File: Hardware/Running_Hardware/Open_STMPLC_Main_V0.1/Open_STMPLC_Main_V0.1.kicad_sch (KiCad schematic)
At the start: 8 parts

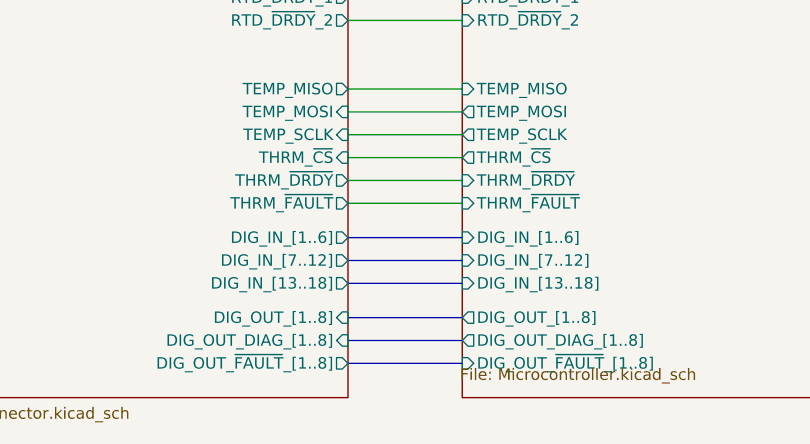
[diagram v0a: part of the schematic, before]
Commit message: Gerber generation v0.1
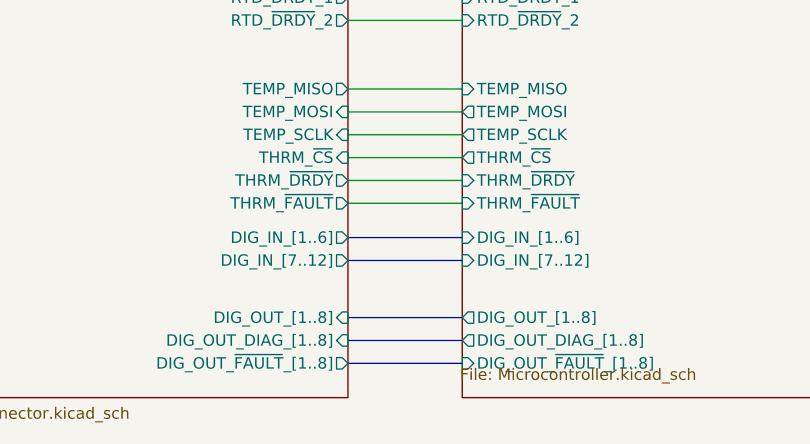
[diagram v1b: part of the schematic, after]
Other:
- sheet B2B_Connector ports: added none; removed DIG_IN_[13..18]
- sheet Microcontroller ports: added none; removed DIG_IN_[13..18]
- company: (none) -> Thingslista Automation LLP
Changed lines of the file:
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@@
 	(title_block
 		(title "Open_STMPLC_Main")
-		(date "2026-05-24")
+		(date "2026-06-03")
 		(rev "0.1")
+		(company "Thingslista Automation LLP")
 	)
 	(bus_alias "SPI"
@@
 		)
 	)
-	(bus
-		(pts
-			(xy 95.25 176.53) (xy 107.95 176.53)
-		)
-		(stroke
-			(width 0)
-			(type default)
-		)
-	)
 	(wire
 		(pts
@@
 			)
 		)
-		(pin "DIG_IN_[13..18]" output
-			(at 95.25 176.53 0)
-			(effects
-				(font
-					(size 1.27 1.27)
-				)
-				(justify right)
-			)
-		)
 		(pin "DIG_OUT_[1..8]" input
 			(at 95.25 180.34 0)
@@
 			(effects
 				(font
-					(size 1.27 1.27)
-				)
-				(justify left)
-			)
-		)
-		(pin "DIG_IN_[13..18]" input
-			(at 107.95 176.53 180)
-			(effects
-				(font
